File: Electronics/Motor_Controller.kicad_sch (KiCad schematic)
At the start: 43 parts, among them J2 SWCLK SWD, SW1 SW_Push, SW2 ~{USB_BOOT}, U1 RP2040, U4 W25Q32JVZP, Y1 ABM8-272-T3

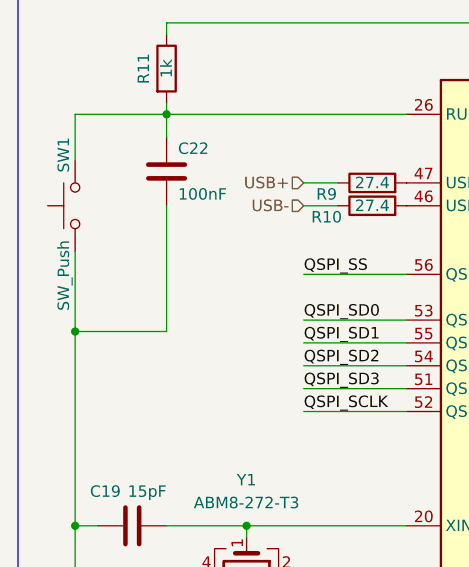
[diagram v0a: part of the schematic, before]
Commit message: started pcb, need bigger frame
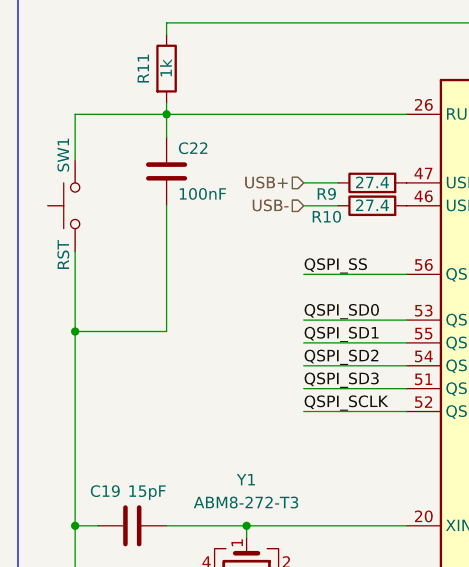
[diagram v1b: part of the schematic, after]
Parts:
- SW1: value SW_Push -> RST
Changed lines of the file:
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@@
       (effects (font (size 1.27 1.27)) (justify right))
     )
-    (property "Value" "SW_Push" (at 17.78 55.88 0)
+    (property "Value" "RST" (at 17.78 55.88 0)
       (effects (font (size 1.27 1.27)) (justify right))
     )
